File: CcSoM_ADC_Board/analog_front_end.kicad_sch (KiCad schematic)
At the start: 20 parts, among them J16 Barrel_Jack, J4 Conn_Coaxial, J6 Conn_01x14, J7 Conn_01x08, J8 Conn_01x16_Socket, J9 Conn_01x08

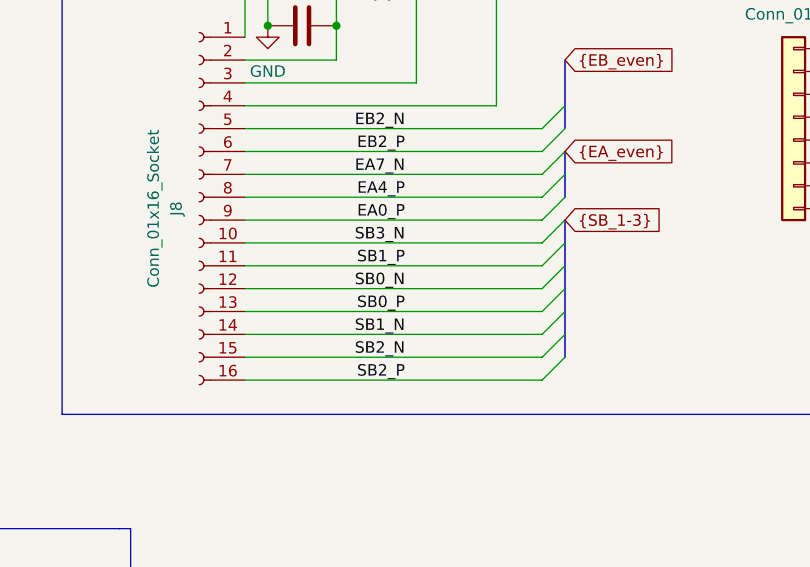
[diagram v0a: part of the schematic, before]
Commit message: changed from 10Bit ADC to 12Bit
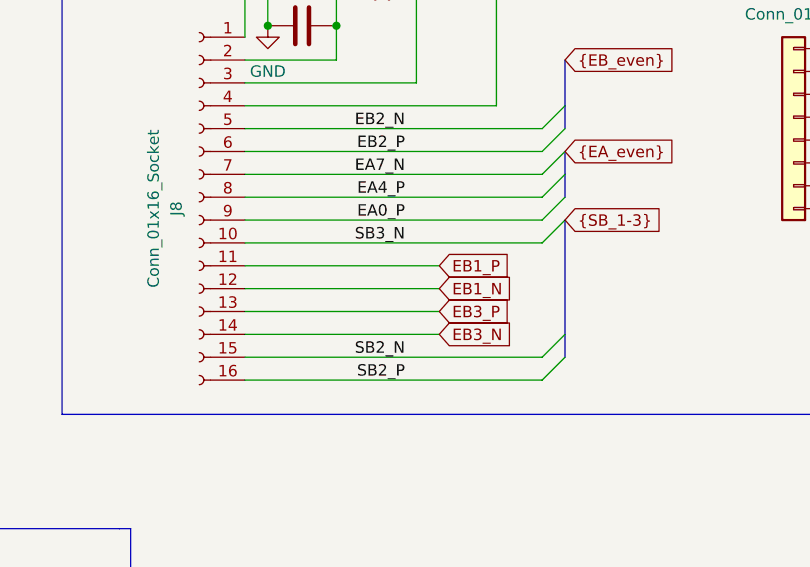
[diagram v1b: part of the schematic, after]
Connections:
- net SB0_N renamed EB1_N
- net SB0_P renamed EB3_P
- net SB1_N renamed EB3_N
- net SB1_P renamed EB1_P
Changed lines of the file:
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@@
-	)
-	(bus_entry
-		(at 224.79 113.03)
-		(size -2.54 2.54)
-		(stroke
-			(width 0)
-			(type default)
-		)
 	)
 	(bus_entry
@@
 	)
 	(bus_entry
-		(at 224.79 110.49)
-		(size -2.54 2.54)
-		(stroke
-			(width 0)
-			(type default)
-		)
-	)
-	(bus_entry
 		(at 224.79 97.79)
 		(size -2.54 2.54)
@@
 	)
 	(bus_entry
-		(at 224.79 107.95)
-		(size -2.54 2.54)
-		(stroke
-			(width 0)
-			(type default)
-		)
-	)
-	(bus_entry
 		(at 269.24 44.45)
 		(size -2.54 2.54)
@@
 		)
 	)
-	(bus_entry
-		(at 224.79 105.41)
-		(size -2.54 2.54)
-		(stroke
-			(width 0)
-			(type default)
-		)
-	)
 	(polyline
 		(pts
@@
 	(wire
 		(pts
+			(xy 189.23 113.03) (xy 210.82 113.03)
+		)
+		(stroke
+			(width 0)
+			(type default)
+		)
+	)
+	(wire
+		(pts
 			(xy 68.58 187.96) (xy 80.01 187.96)
 		)
@@
 	(bus
 		(pts
-			(xy 224.79 105.41) (xy 224.79 107.95)
+			(xy 224.79 102.87) (xy 224.79 115.57)
 		)
 		(stroke
@@
 		(pts
 			(xy 191.77 76.2) (xy 200.66 76.2)
-		)
-		(stroke
-			(width 0)
-			(type default)
-		)
-	)
-	(wire
-		(pts
-			(xy 189.23 110.49) (xy 222.25 110.49)
 		)
 		(stroke
@@
 		)
 	)
-	(bus
-		(pts
-			(xy 224.79 110.49) (xy 224.79 113.03)
-		)
-		(stroke
-			(width 0)
-			(type default)
-		)
-	)
-	(wire
-		(pts
-			(xy 189.23 113.03) (xy 222.25 113.03)
-		)
-		(stroke
-			(width 0)
-			(type default)
-		)
-	)
 	(wire
 		(pts
@@
 	(wire
 		(pts
-			(xy 189.23 107.95) (xy 222.25 107.95)
-		)
-		(stroke
-			(width 0)
-			(type default)
-		)
-	)
-	(wire
-		(pts
 			(xy 250.19 39.37) (xy 266.7 39.37)
 		)
@@
 		(pts
 			(xy 224.79 95.25) (xy 224.79 97.79)
-		)
-		(stroke
-			(width 0)
-			(type default)
-		)
-	)
-	(wire
-		(pts
-			(xy 189.23 115.57) (xy 222.25 115.57)
 		)
 		(stroke
@@
 		)
 	)
-	(bus
-		(pts
-			(xy 224.79 102.87) (xy 224.79 105.41)
+	(wire
+		(pts
+			(xy 189.23 107.95) (xy 210.82 107.95)
 		)
 		(stroke
@@
 		)
 	)
+	(wire
+		(pts
+			(xy 189.23 115.57) (xy 210.82 115.57)
+		)
+		(stroke
+			(width 0)
+			(type default)
+		)
+	)
+	(wire
+		(pts
+			(xy 189.23 110.49) (xy 210.82 110.49)
+		)
+		(stroke
+			(width 0)
+			(type default)
+		)
+	)
 	(bus
 		(pts
 			(xy 269.24 29.21) (xy 269.24 31.75)
-		)
-		(stroke
-			(width 0)
-			(type default)
-		)
-	)
-	(bus
-		(pts
-			(xy 224.79 107.95) (xy 224.79 110.49)
-		)
-		(stroke
-			(width 0)
-			(type default)
-		)
-	)
-	(bus
-		(pts
-			(xy 224.79 113.03) (xy 224.79 115.57)
 		)
 		(stroke
@@
 		)
 	)
-	(label "SB1_N"
-		(at 207.01 115.57 180)
-		(effects
-			(font
-				(size 1.27 1.27)
-			)
-			(justify right bottom)
-		)
-	)
 	(label "NB4_P"
 		(at 264.16 93.98 180)
@@
 		)
 	)
-	(label "SB0_N"
-		(at 207.01 110.49 180)
-		(effects
-			(font
-				(size 1.27 1.27)
-			)
-			(justify right bottom)
-		)
-	)
 	(label "NB4_N"
 		(at 203.2 43.18 180)
@@
 		)
 	)
-	(label "SB1_P"
-		(at 207.01 107.95 180)
-		(effects
-			(font
-				(size 1.27 1.27)
-			)
-			(justify right bottom)
-		)
-	)
 	(label "NB6_N"
 		(at 203.2 38.1 180)
@@
 		)
 	)
-	(label "SB0_P"
-		(at 207.01 113.03 180)
-		(effects
-			(font
-				(size 1.27 1.27)
-			)
-			(justify right bottom)
-		)
-	)
 	(label "NA3_P"
 		(at 203.2 58.42 180)
@@
 			)
 			(justify right bottom)
+		)
+	)
+	(global_label "EB1_P"
+		(shape input)
+		(at 210.82 107.95 0)
+		(fields_autoplaced yes)
+		(effects
+			(font
+				(size 1.27 1.27)
+			)
+			(justify left)
+		)
+		(property "Intersheetrefs" "${INTERSHEET_REFS}"
+			(at 219.6713 107.95 0)
+			(effects
+				(font
+					(size 1.27 1.27)
+				)
+				(justify left)
+				(hide yes)
+			)
 		)
 	)
@@
 		)
 	)
+	(global_label "EB1_N"
+		(shape input)
+		(at 210.82 110.49 0)
+		(fields_autoplaced yes)
+		(effects
+			(font
+				(size 1.27 1.27)
+			)
+			(justify left)
+		)
+		(property "Intersheetrefs" "${INTERSHEET_REFS}"
+			(at 219.7318 110.49 0)
+			(effects
+				(font
+					(size 1.27 1.27)
+				)
+				(justify left)
+				(hide yes)
+			)
+		)
+	)
 	(global_label "{NB_even}"
 		(shape input)
@@
 		)
 	)
+	(global_label "EB3_N"
+		(shape input)
+		(at 210.82 115.57 0)
+		(fields_autoplaced yes)
+		(effects
+			(font
+				(size 1.27 1.27)
+			)
+			(justify left)
+		)
+		(property "Intersheetrefs" "${INTERSHEET_REFS}"
+			(at 219.7318 115.57 0)
+			(effects
+				(font
+					(size 1.27 1.27)
+				)
+				(justify left)
+				(hide yes)
+			)
+		)
+	)
 	(global_label "{SB_1-3}"
 		(shape input)
@@
 			(effects
 				(font
+					(size 1.27 1.27)
+				)
+				(justify left)
+				(hide yes)
+			)
+		)
+	)
+	(global_label "EB3_P"
+		(shape input)
+		(at 210.82 113.03 0)
+		(fields_autoplaced yes)
+		(effects
+			(font
+				(size 1.27 1.27)
+			)
+			(justify left)
+		)
+		(property "Intersheetrefs" "${INTERSHEET_REFS}"
+			(at 219.6713 113.03 0)
+			(effects
+				(font

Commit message: corrected schematic created pdf and bom file
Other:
- company: (none) -> Technische Hochschule Köln
- title: (none) -> SoM Programmer & ADC Board
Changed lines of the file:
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@@
 	(generator_version "9.0")
 	(paper "A4")
+	(title_block
+		(title "SoM Programmer & ADC Board")
+		(date "2026-02-09")
+		(rev "0.1")
+		(company "Technische Hochschule Köln")
+	)
 	(bus_alias "EA_even"
 		(members "EA0_N" "EA0_P" "EA2_N" "EA2_P" "EA4_N" "EA4_P" "EA7_N" "EA7_P")

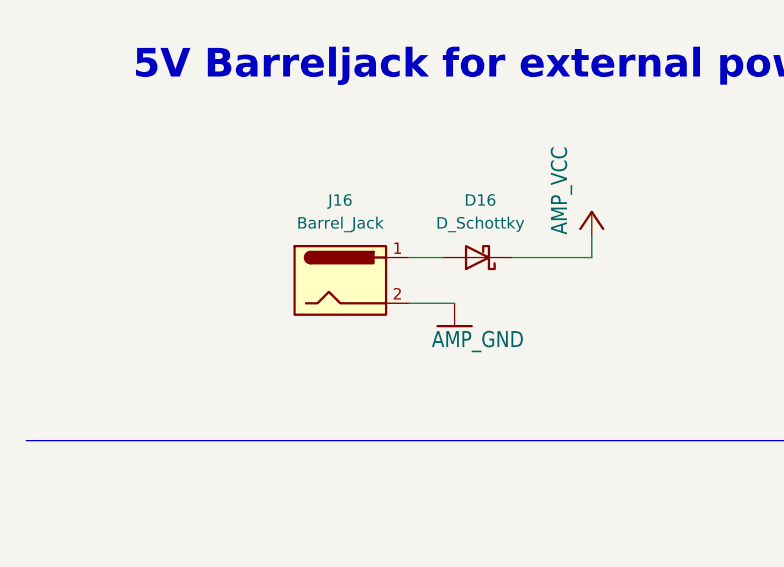
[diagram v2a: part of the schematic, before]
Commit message: changed schottky, began to add digikey part numbers
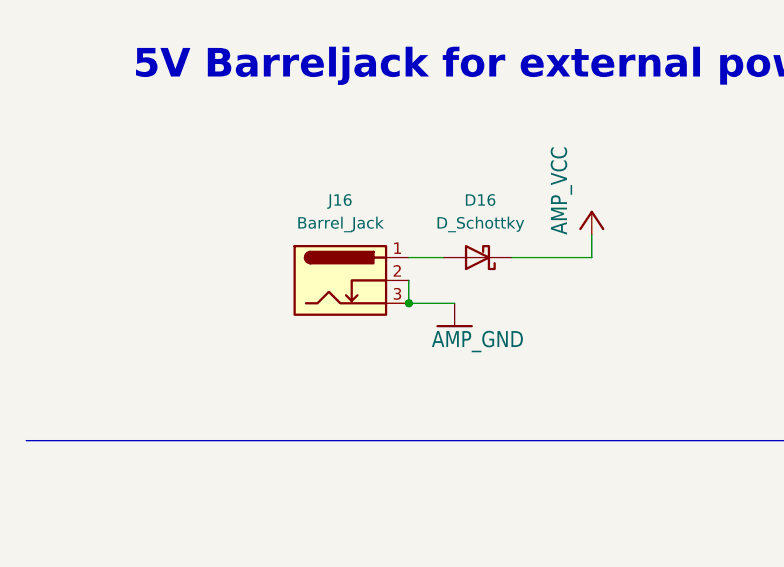
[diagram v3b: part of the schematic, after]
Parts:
- D16: footprint Diode_SMD:D_0603_1608Metric_Pad1.05x0.95mm_HandSolder -> Diode_SMD:D_0805_2012Metric_Pad1.15x1.40mm_HandSolder; DigiKey_no (none) -> 478-7800-1-ND
- J16: symbol Connector:Barrel_Jack -> Connector:Barrel_Jack_Switch_Pin3Ring; DigiKey_no (none) -> 4654-FC681465S-ND
- R46, R48: DigiKey_no (none) -> 478-UBR0402B250FZTR\500CT-ND
- R49: DigiKey_no (none) -> 541-10.0LCT-ND
- R50, R51: DigiKey_no (none) -> 846-MCR01SMQPF12R0CT-ND
- TR1: DigiKey_no (none) -> 3157-T1-1T-KK81+CT-ND
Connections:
- net ADC_GND_ANALOG: now also J16.3
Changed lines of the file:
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@@
 	)
 	(junction
+		(at 54.61 60.96)
+		(diameter 0)
+		(color 0 0 0 0)
+	)
+	(junction
 		(at 217.17 73.66)
 		(diameter 0)
@@
 	(wire
 		(pts
+			(xy 54.61 58.42) (xy 54.61 60.96)
+		)
+		(stroke
+			(width 0)
+			(type default)
+		)
+	)
+	(wire
+		(pts
 			(xy 190.5 43.18) (xy 203.2 43.18)
 		)
@@
 			)
 		)
-		(property "Footprint" "Diode_SMD:D_0603_1608Metric_Pad1.05x0.95mm_HandSolder"
+		(property "Footprint" "Diode_SMD:D_0805_2012Metric_Pad1.15x1.40mm_HandSolder"
 			(at 62.23 55.88 0)
 			(effects
@@
 			)
 		)
-		(property "Datasheet" "~"
+		(property "Datasheet" "https://datasheets.kyocera-avx.com/schottky.pdf"
 			(at 62.23 55.88 0)
 			(effects
@@
 			)
 		)
+		(property "DigiKey_no" "478-7800-1-ND"
+			(at 62.23 55.88 0)
+			(effects
+				(font
+					(size 1.27 1.27)
+				)
+				(hide yes)
+			)
+		)
 		(pin "1"
 		)
@@
 			)
 		)
+		(property "DigiKey_no" "846-MCR01SMQPF12R0CT-ND"
+			(at 85.09 187.96 0)
+			(effects
+				(font
+					(size 1.27 1.27)
+				)
+				(hide yes)
+			)
+		)
 		(pin "1"
 		)
@@
 			)
 		)
+		(property "DigiKey_no" "541-10.0LCT-ND"
+			(at 83.82 144.78 0)
+			(effects
+				(font
+					(size 1.27 1.27)
+				)
+				(hide yes)
+			)
+		)
 		(pin "1"
 		)
@@
 	)
 	(symbol
-		(lib_id "Connector:Barrel_Jack")
+		(lib_id "Connector:Barrel_Jack_Switch_Pin3Ring")
 		(at 46.99 58.42 0)
 		(unit 1)
@@
 			)
 		)
-		(property "Description" "DC Barrel Jack"
+		(property "Description" "DC Barrel Jack with an internal switch"
+			(at 46.99 58.42 0)
+			(effects
+				(font
+					(size 1.27 1.27)
+				)
+				(hide yes)
+			)
+		)
+		(property "DigiKey_no" "4654-FC681465S-ND"
 			(at 46.99 58.42 0)
 			(effects
@@
 		(pin "1"
 		)
+		(pin "3"
+		)
 		(instances
 			(project "SoMProgrammerNTester"
@@
 			)
 		)
+		(property "DigiKey_no" "478-UBR0402B250FZTR\\500CT-ND"
+			(at 68.58 182.88 0)
+			(effects
+				(font
+					(size 1.27 1.27)
+				)
+				(hide yes)
+			)
+		)
 		(pin "1"
 		)
@@
 			)
 		)
+		(property "DigiKey_no" "478-UBR0402B250FZTR\\500CT-ND"
+			(at 68.58 168.91 0)
+			(effects
+				(font
+					(size 1.27 1.27)
+				)
+				(hide yes)
+			)
+		)
 		(pin "1"
 		)
@@
 			)
 		)
+		(property "DigiKey_no" "846-MCR01SMQPF12R0CT-ND"
+			(at 85.09 163.83 0)
+			(effects
+				(font
+					(size 1.27 1.27)
+				)
+				(hide yes)
+			)
+		)
 		(pin "1"
 		)
@@
 			(effects
 				(font
+					(size 1.27 1.27)
+				)
+				(hide yes)
+			)
+		)
+		(property "DigiKey_no" "3157-T1-1T-KK81+CT-ND "
+			(at 54.61 175.26 0)
+			(effects
+				(font

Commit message: digikey no not complete
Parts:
- C55, C56: DigiKey_no (none) -> C0402C104K4RACTU
- C57: DigiKey_no (none) -> 490-10012-1-ND
- C58: DigiKey_no (none) -> 399-C0402C120J5GACTUCT-ND
- C60, C61, C62: DigiKey_no (none) -> 399-C0603C105K4RACTUCT-ND
- J4: DigiKey_no (none) -> ACX1995-ND
- J6: DigiKey_no (none) -> S7012-ND
- J7, J9: DigiKey_no (none) -> S7006-ND
- J8: DigiKey_no (none) -> S7014-ND
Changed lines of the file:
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@@
+			)
+		)
+		(property "DigiKey_no" "ACX1995-ND"
+			(at 30.48 170.18 0)
+			(effects
+				(font
+					(size 1.27 1.27)
+				)
+				(hide yes)
 			)
 		)
@@
 			)
 		)
+		(property "DigiKey_no" "S7014-ND"
+			(at 184.15 100.33 90)
+			(effects
+				(font
+					(size 1.27 1.27)
+				)
+				(hide yes)
+			)
+		)
 		(pin "14"
 		)
@@
 			)
 		)
+		(property "DigiKey_no" "S7012-ND"
+			(at 185.42 48.26 0)
+			(effects
+				(font
+					(size 1.27 1.27)
+				)
+				(hide yes)
+			)
+		)
 		(pin "10"
 		)
@@
 		)
 		(property "Description" ""
+			(at 106.68 177.8 0)
+			(effects
+				(font
+					(size 1.27 1.27)
+				)
+				(hide yes)
+			)
+		)
+		(property "DigiKey_no" "399-C0402C120J5GACTUCT-ND"
 			(at 106.68 177.8 0)
 			(effects
@@
 			)
 		)
+		(property "DigiKey_no" "399-C0603C105K4RACTUCT-ND"
+			(at 195.58 81.28 90)
+			(effects
+				(font
+					(size 1.27 1.27)
+				)
+				(hide yes)
+			)
+		)
 		(pin "1"
 		)
@@
 			)
 		)
+		(property "DigiKey_no" "399-C0603C105K4RACTUCT-ND"
+			(at 213.36 73.66 90)
+			(effects
+				(font
+					(size 1.27 1.27)
+				)
+				(hide yes)
+			)
+		)
 		(pin "1"
 		)
@@
 			)
 		)
+		(property "DigiKey_no" "490-10012-1-ND"
+			(at 92.71 149.86 0)
+			(effects
+				(font
+					(size 1.27 1.27)
+				)
+				(hide yes)
+			)
+		)
 		(pin "1"
 		)
@@
 			)
 		)
+		(property "DigiKey_no" "399-C0603C105K4RACTUCT-ND"
+			(at 204.47 76.2 90)
+			(effects
+				(font
+					(size 1.27 1.27)
+				)
+				(hide yes)
+			)
+		)
 		(pin "1"
 		)
@@
 		)
 		(property "Description" ""
+			(at 38.1 170.18 0)
+			(effects
+				(font
+					(size 1.27 1.27)
+				)
+				(hide yes)
+			)
+		)
+		(property "DigiKey_no" "C0402C104K4RACTU"
 			(at 38.1 170.18 0)
 			(effects
@@
 			)
 		)
+		(property "DigiKey_no" "S7006-ND"
+			(at 245.11 41.91 0)
+			(effects
+				(font
+					(size 1.27 1.27)
+				)
+				(hide yes)
+			)
+		)
 		(pin "2"
 		)
@@
 			)
 		)
+		(property "DigiKey_no" "S7006-ND"
+			(at 250.19 93.98 0)
+			(effects
+				(font
+					(size 1.27 1.27)
+				)
+				(hide yes)
+			)
+		)
 		(pin "4"
 		)
@@
 			(at 78.74 175.26 0)
 			(effects
+				(font
+					(size 1.27 1.27)
+				)
+				(hide yes)
+			)
+		)
+		(property "DigiKey_no" "C0402C104K4RACTU"
+			(at 78.74 175.26 0)
+			(effects

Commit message: changed digikeyno from component, added info into readme about discontinued parts in digikey
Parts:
- R50, R51: DigiKey_no 846-MCR01SMQPF12R0CT-ND -> YAG2968CT-ND
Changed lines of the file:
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@@
 			)
 		)
-		(property "DigiKey_no" "846-MCR01SMQPF12R0CT-ND"
+		(property "DigiKey_no" "YAG2968CT-ND"
 			(at 85.09 187.96 0)
 			(effects
@@
 			)
 		)
-		(property "DigiKey_no" "846-MCR01SMQPF12R0CT-ND"
+		(property "DigiKey_no" "YAG2968CT-ND"
 			(at 85.09 163.83 0)
 			(effects
